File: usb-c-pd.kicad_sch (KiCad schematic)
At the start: 1 part, among them U1 CYPD3177-24LQ

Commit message: feat: add primary components
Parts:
- added J1: USB_C_Receptacle_PowerOnly_6P, symbol Connector:USB_C_Receptacle_PowerOnly_6P
- added J2: Barrel_Jack, symbol Connector:Barrel_Jack
- added U2: STM32G030K8Tx, Package_QFP:LQFP-32_7x7mm_P0.8mm, symbol MCU_ST_STM32G0:STM32G030K8Tx
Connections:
- new net: J1.A12 (GND), J1.B12 (GND)
- new net: J1.A9 (VBUS), J1.B9 (VBUS)
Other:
- moved on the sheet: U1

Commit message: feat: ez-pd
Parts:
- removed J2: Barrel_Jack, symbol Connector:Barrel_Jack
- added C1, C2: 1uF, symbol Device:C_Small
- added C3, C4: 0.1uF, symbol Device:C_Small
- added C5, C6: 4.7uF, symbol Device:C_Small
- added C7, C8, C9: 100nF, symbol Device:C_Small
- added D1: LED, symbol Device:LED
- added J2: Barrel_Jack_Switch, symbol Connector:Barrel_Jack_Switch
- added Q1: T2N7002AK, Package_TO_SOT_SMD:SOT-23, symbol Transistor_FET:T2N7002AK
- added Q2: ~, usb-c-pd-lib:SOIC127P600X175-8N, symbol usb-c-pd-prodj-lib:DMP3098LSD-13
- added R1, R3, R4: 4.7k, symbol Device:R_Small
- added R10, R11, R13, R15, R16, R17, R19, R6, R7, R8, R9: 2.2k, symbol Device:R_Small
- added R12: DNP, symbol Device:R_Small
- added R14: 20k, symbol Device:R_Small
- added R18: 12mR, symbol Device:R_Small
- added R2, R5: TODO, symbol Device:R_Small
- added U3: INA180A3, Package_TO_SOT_SMD:SOT-23-5, symbol Amplifier_Current:INA180A3
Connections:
- net VBUX_MIN: now reaches U1.1 (VBUS_MIN)
- net VBUX_MIN: now also R8.2, R9.1
- net at U1.10 (FLIP): now also R1.1
- net +VBUS_PD: now reaches U1.11 (VDC_OUT)
- net +VBUS_PD: now also C7.1, Q2.5 (D2), Q2.6 (D2), R18.2, U3.3 (+)
- net at U1.12 (HPI_SDA): now also R4.2
- net at U1.13 (HPI_SCL): now also R3.2
- net at U1.14 (CC2): now also J1.B5 (CC2)
- net at U1.15 (CC1): now also J1.A5 (CC1)
- net VBUS: now reaches U1.18 (VBUS_IN)
- net VBUS: now also J1.A9 (VBUS), J1.B9 (VBUS), C6.1, D1.2 (A), Q2.7 (D), Q2.8 (D), R14.1
- net GND: now reaches U1.19 (GND), U1.22 (GND), U1.25 (GND)
- net GND: now also J1.A12 (GND), J1.B12 (GND), J1.S1 (SHIELD), C1.2, C2.2, C3.2, C4.2, C5.2, C8.2, C9.1, J2.2, J2.3, Q1.2 (S), R11.2, R13.2, R5.1, R7.2, R9.2, U3.2 (GND)
- net VBUX_MAX: now reaches U1.2 (VBUS_MAX)
- net VBUX_MAX: now also R6.2, R7.1
- net +3V3: now reaches U1.23 (VDDD)
- net +3V3: now also C2.1, C3.1, C4.1, R1.2, R3.1, R4.1
- net at U1.24 (VCCD): now also C1.1
- net VBUS_FET_EN: now reaches U1.3 (VBUS_FET_EN)
- net VBUS_FET_EN: now also R16.2
- net at U1.4 (SAFE_PWR_EN): now also R17.1
- net ISINK_COARSE: now reaches U1.5 (ISNK_COARSE)
- net ISINK_COARSE: now also R10.2, R11.1
- net ISINK_FINE: now reaches U1.6 (ISNK_FINE)
- net ISINK_FINE: now also R12.2, R13.1
- net at U1.9 (FAULT): now also Q1.1 (G), R5.2
- new net: Q1.3 (D), R2.1
- new net: Q2.1 (S1), Q2.3 (S2)
- new net: Q2.2 (G1), Q2.4 (G2), R15.1
- new net: D1.1 (K), R2.2
- new net: R19.1, U3.1
- new net: C6.2, C7.2, R14.2, R15.2, R16.1
- new net +3V3 MCU: C8.1, R10.1, R12.1, R6.1, R8.1, U3.5 (V+)
- new net AMP_OUT: C9.2, R19.2
- new net PD_SAFE: R17.2
- new net VCONN: C5.1, J2.1, R18.1, U3.4 (-)
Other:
- note added: "ISINK = 3V3 * 0/2 -> 0A"
- note added: "ISINK = 3V3/2 -> 3A"
- note added: "VBUX_MAX = 3V3/2 -> 15V"
- note added: "VBUX_MIN = 3V3/2 -> 15V"
- note added: "Verify that this transistor is in stock"
- moved on the sheet: J1, U1

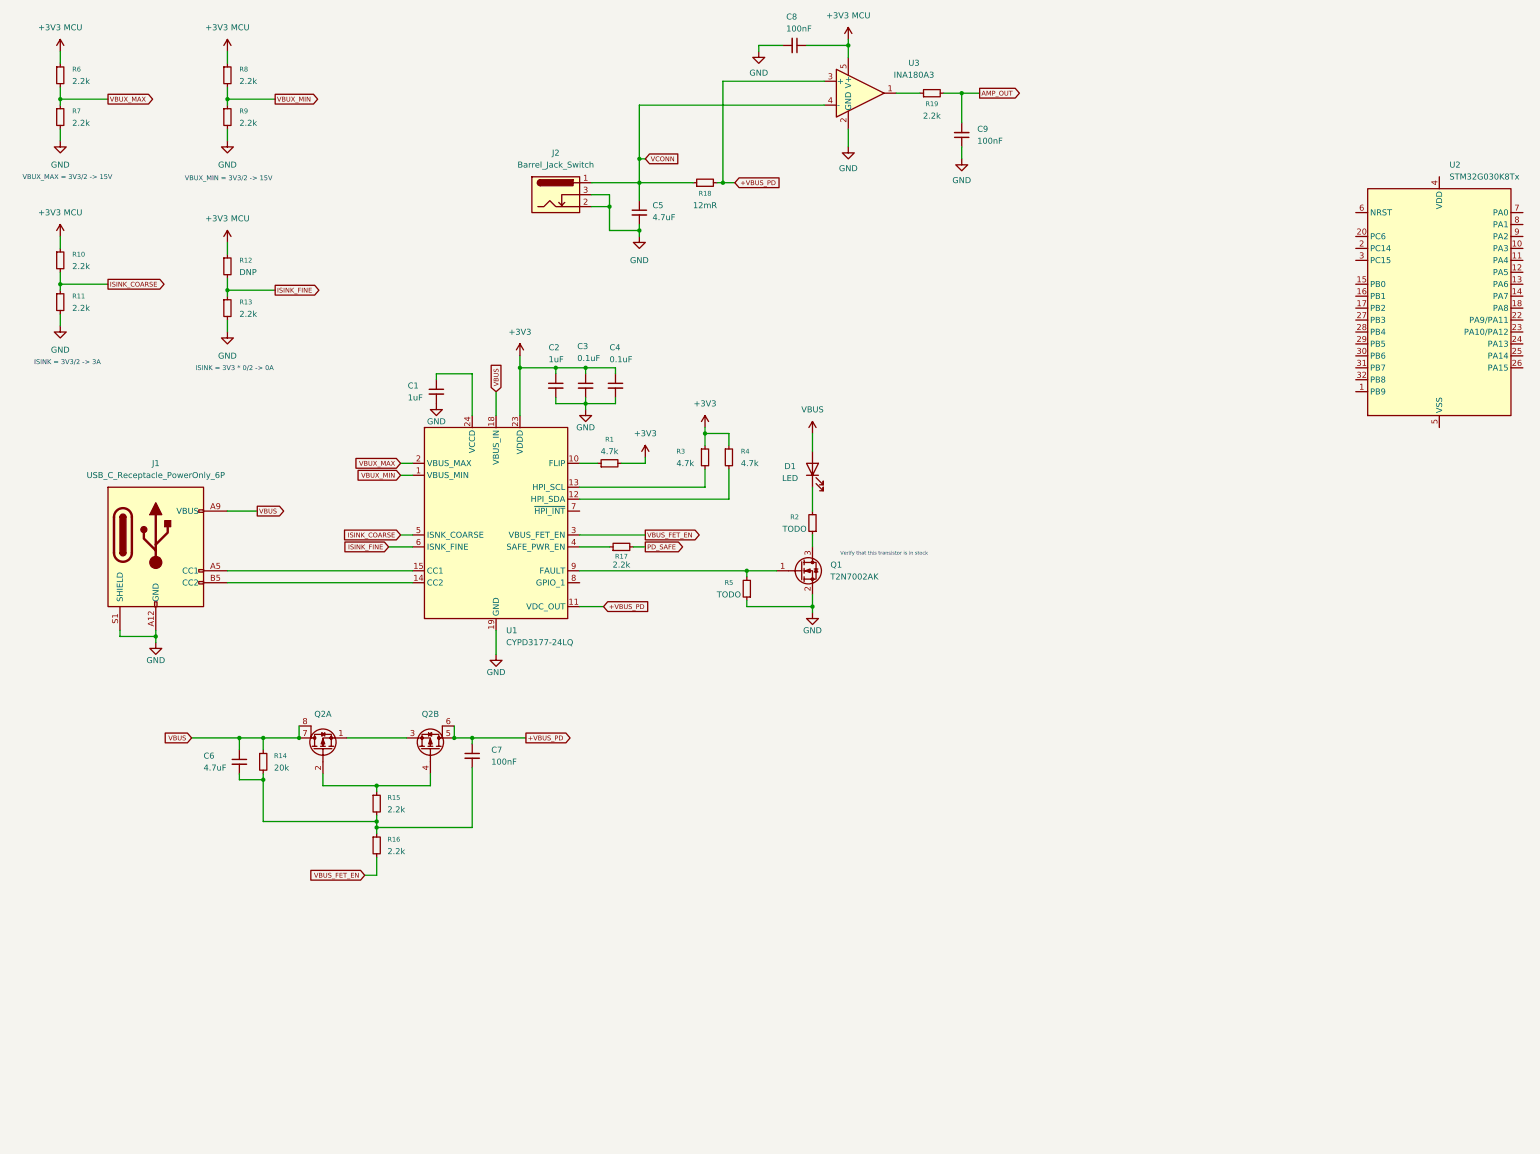
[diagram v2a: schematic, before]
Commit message: feat: mcu (#1)
* feat: stm mcu

* feat: SWO programming

* verify ERC
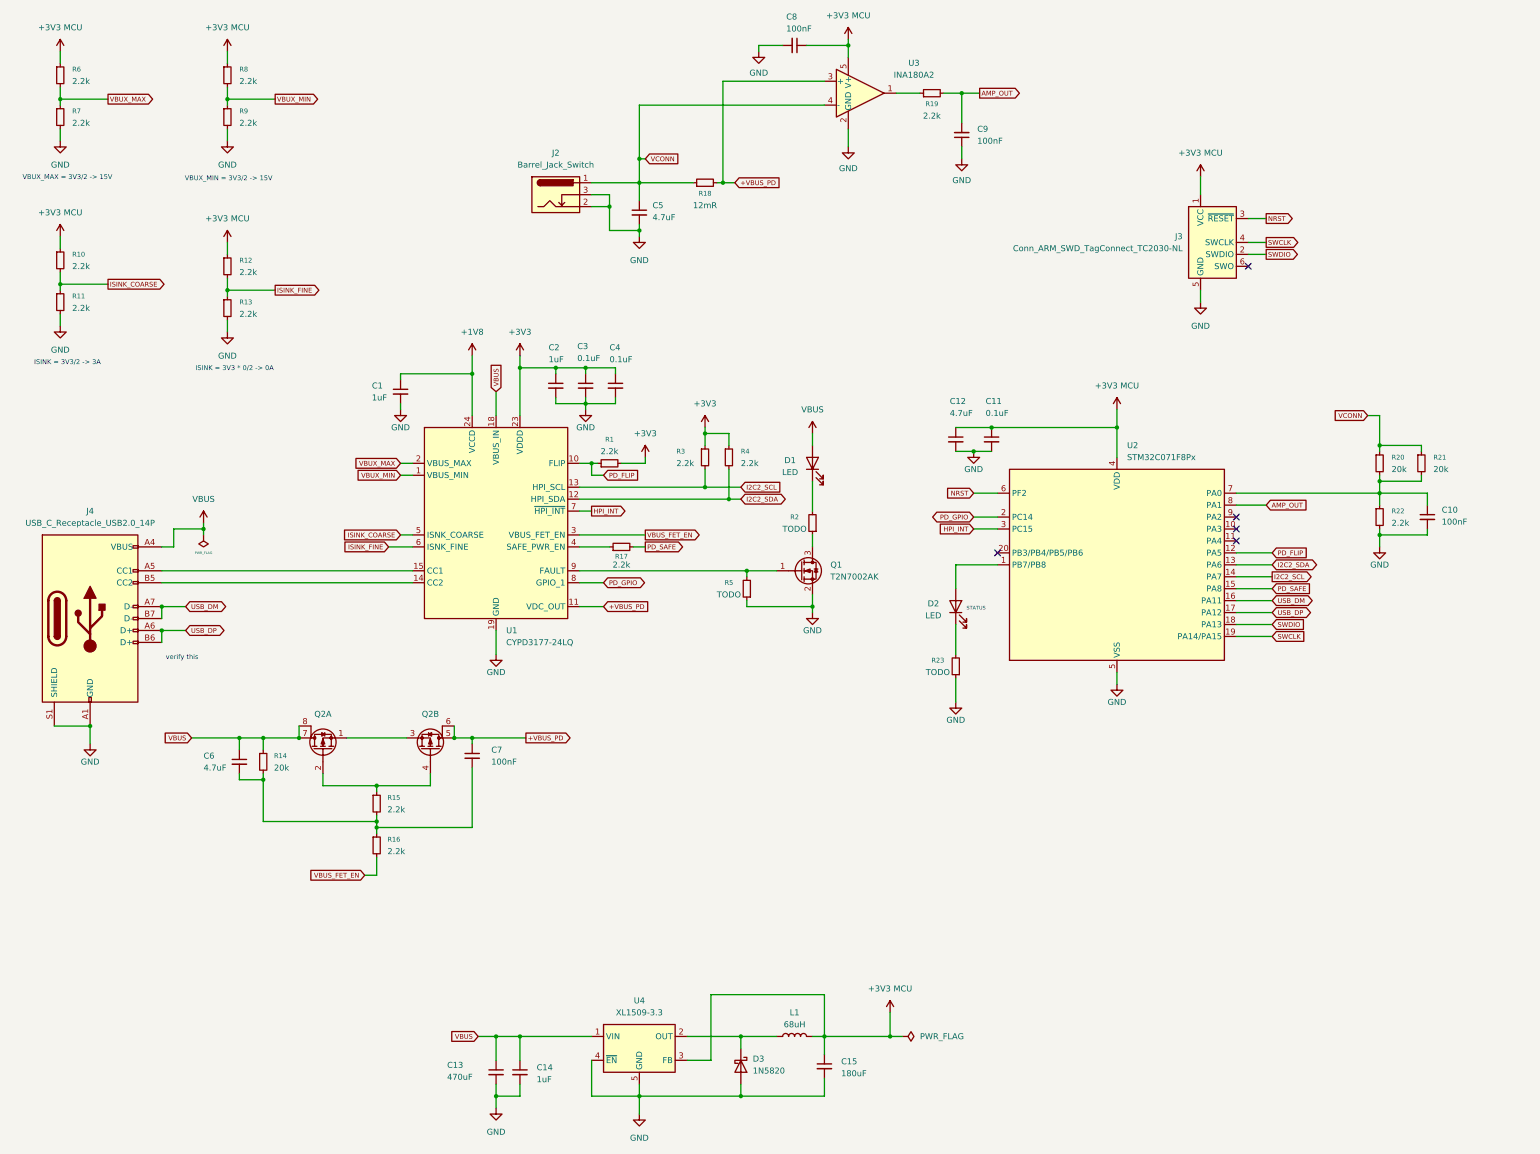
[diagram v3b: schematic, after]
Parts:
- removed J1: USB_C_Receptacle_PowerOnly_6P, symbol Connector:USB_C_Receptacle_PowerOnly_6P
- removed U2: STM32G030K8Tx, Package_QFP:LQFP-32_7x7mm_P0.8mm, symbol MCU_ST_STM32G0:STM32G030K8Tx
- removed U3: INA180A3, Package_TO_SOT_SMD:SOT-23-5, symbol Amplifier_Current:INA180A3
- added C10: 100nF, symbol Device:C_Small
- added C11: 0.1uF, symbol Device:C_Small
- added C12: 4.7uF, symbol Device:C_Small
- added C13: 470uF, symbol Device:C_Small
- added C14: 1uF, symbol Device:C_Small
- added C15: 180uF, symbol Device:C_Small
- added D2: LED, symbol Device:LED
- added D3: 1N5820, Diode_THT:D_DO-201AD_P15.24mm_Horizontal, symbol Diode:1N5820
- added J3: Conn_ARM_SWD_TagConnect_TC2030-NL, Connector:Tag-Connect_TC2030-IDC-NL_2x03_P1.27mm_Vertical, symbol Connector:Conn_ARM_SWD_TagConnect_TC2030-NL
- added J4: USB_C_Receptacle_USB2.0_14P, symbol Connector:USB_C_Receptacle_USB2.0_14P
- added L1: 68uH, symbol Device:L
- added R20, R21: 20k, Resistor_SMD:R_0603_1608Metric_Pad0.98x0.95mm_HandSolder, symbol Device:R_Small
- added R22: 2.2k, Resistor_SMD:R_0603_1608Metric_Pad0.98x0.95mm_HandSolder, symbol Device:R_Small
- added R23: TODO, Resistor_SMD:R_0603_1608Metric_Pad0.98x0.95mm_HandSolder, symbol Device:R_Small
- added U2: STM32C071F8Px, Package_SO:TSSOP-20_4.4x6.5mm_P0.65mm, symbol MCU_ST_STM32C0:STM32C071F8Px
- added U3: INA180A2, Package_TO_SOT_SMD:SOT-23-5, symbol Amplifier_Current:INA180A2
- added U4: XL1509-3.3, Package_SO:SOIC-8_3.9x4.9mm_P1.27mm, symbol Regulator_Switching:XL1509-3.3
- R1, R3, R4: value 4.7k -> 2.2k; footprint (none) -> Resistor_SMD:R_0603_1608Metric_Pad0.98x0.95mm_HandSolder
- R10, R11, R13, R14, R15, R16, R17, R19, R2, R5, R6, R7, R8, R9: footprint (none) -> Resistor_SMD:R_0603_1608Metric_Pad0.98x0.95mm_HandSolder
- R12: value DNP -> 2.2k; footprint (none) -> Resistor_SMD:R_0603_1608Metric_Pad0.98x0.95mm_HandSolder
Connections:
- net +3V3 MCU: now also C11.1, C12.1, C15.1, J3.1 (VCC), L1.2, U2.4 (VDD), U3.5 (V+), U4.3 (FB)
- net +VBUS_PD: now also U3.3 (+)
- net AMP_OUT: now also U2.8 (PA1)
- net GND: now also C10.2, C11.2, C12.2, C13.2, C14.2, C15.2, D3.2 (A), J3.5 (GND), J4.A1 (GND), J4.A12 (GND), J4.B1 (GND), J4.B12 (GND), J4.S1 (SHIELD), R22.2, R23.1, U2.5 (VSS), U3.2 (GND), U4.4 (~{EN}), U4.5 (GND), U4.6 (GND), U4.7 (GND), U4.8 (GND)
- net PD_SAFE: now also U2.15 (PA8)
- net VBUS: now also C13.1, C14.1, J4.A4 (VBUS), J4.A9 (VBUS), J4.B4 (VBUS), J4.B9 (VBUS), U4.1 (VIN)
- net VCONN: now also R20.1, R21.1, U3.4 (-)
- net I2C2_SDA: now reaches R4.2, U1.12 (HPI_SDA)
- net I2C2_SDA: now also U2.13 (PA6)
- net +1V8: now reaches C1.1, U1.24 (VCCD)
- net PD_FLIP: now reaches R1.1, U1.10 (FLIP)
- net PD_FLIP: now also U2.12 (PA5)
- net at R19.1: now also U3.1
- net I2C2_SCL: now reaches R3.2, U1.13 (HPI_SCL)
- net I2C2_SCL: now also U2.14 (PA7)
- net at U1.14 (CC2): now also J4.B5 (CC2)
- net at U1.15 (CC1): now also J4.A5 (CC1)
- net HPI_INT: now reaches U1.7 (~{HPI_INT})
- net HPI_INT: now also U2.3 (PC15)
- net PD_GPIO: now reaches U1.8 (GPIO_1)
- net PD_GPIO: now also U2.2 (PC14)
- new net: C10.1, R20.2, R21.2, R22.1, U2.7 (PA0)
- new net: D2.1 (K), R23.2
- new net: D2.2 (A), U2.1 (PB7/PB8)
- new net: D3.1 (K), L1.1, U4.2 (OUT)
- new net NRST: J3.3 (~{RESET}), U2.6 (PF2)
- new net SWCLK: J3.4 (SWCLK), U2.19 (PA14/PA15)
- new net SWDIO: J3.2 (SWDIO), U2.18 (PA13)
- new net USB_DM: J4.A7 (D-), J4.B7 (D-), U2.16 (PA11)
- new net USB_DP: J4.A6 (D+), J4.B6 (D+), U2.17 (PA12)
- no-connect marks 0 -> 5
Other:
- note added: "STATUS"
- note added: "verify this"
- note removed: "Verify that this transistor is in stock"
- moved on the sheet: C1, D1

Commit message: feat: configure footprints
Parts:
- C1, C11, C12, C13, C14, C15, C2, C3, C4, C5, C6: footprint (none) -> Capacitor_SMD:C_0603_1608Metric_Pad1.08x0.95mm_HandSolder
- C10, C7, C8, C9: value 100nF -> 0.1uF; footprint (none) -> Capacitor_SMD:C_0603_1608Metric_Pad1.08x0.95mm_HandSolder
- D1, D2: footprint (none) -> Diode_SMD:D_0603_1608Metric_Pad1.05x0.95mm_HandSolder
- J2: footprint (none) -> usb-c-pd-lib:PJ002AHSMTTR
- L1: footprint (none) -> Inductor_SMD:L_0603_1608Metric_Pad1.05x0.95mm_HandSolder
- R18: footprint (none) -> Resistor_SMD:R_0603_1608Metric_Pad0.98x0.95mm_HandSolder
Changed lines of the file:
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@@
 		)
 	)
-	(global_label "VBUS"
-		(shape input)
-		(at 119.38 97.79 90)
-		(fields_autoplaced yes)
-		(effects
-			(font
-				(size 1.016 1.016)
-			)
-			(justify left)
-		)
-		(property "Intersheetrefs" "${INTERSHEET_REFS}"
-			(at 119.38 91.4832 90)
-			(effects
-				(font
-					(size 1.27 1.27)
-				)
-				(justify left)
-				(hide yes)
-			)
-		)
-	)
 	(global_label "HPI_INT"
 		(shape output)
@@
 			)
 		)
-		(property "Footprint" ""
+		(property "Footprint" "Capacitor_SMD:C_0603_1608Metric_Pad1.08x0.95mm_HandSolder"
 			(at 138.43 96.52 0)
 			(effects
@@
 			)
 		)
-		(property "Footprint" ""
+		(property "Footprint" "Capacitor_SMD:C_0603_1608Metric_Pad1.08x0.95mm_HandSolder"
 			(at 99.06 97.79 0)
 			(effects
@@
 			)
 		)
-		(property "Footprint" ""
+		(property "Footprint" "Diode_SMD:D_0603_1608Metric_Pad1.05x0.95mm_HandSolder"
 			(at 217.17 143.51 0)
 			(effects
@@
 			)
 		)
-		(property "Value" "100nF"
+		(property "Value" "0.1uF"
 			(at 181.102 20.574 90)
 			(effects
@@
 			)
 		)
-		(property "Footprint" ""
+		(property "Footprint" "Capacitor_SMD:C_0603_1608Metric_Pad1.08x0.95mm_HandSolder"
 			(at 182.88 24.13 0)
 			(effects
@@
 			)
 		)
-		(property "Value" "100nF"
+		(property "Value" "0.1uF"
 			(at 320.548 125.476 0)
 			(effects
@@
 			)
 		)
-		(property "Footprint" ""
+		(property "Footprint" "Capacitor_SMD:C_0603_1608Metric_Pad1.08x0.95mm_HandSolder"
 			(at 317.5 124.46 0)
 			(effects
@@
 			)
 		)
-		(property "Footprint" ""
+		(property "Footprint" "Capacitor_SMD:C_0603_1608Metric_Pad1.08x0.95mm_HandSolder"
 			(at 217.17 107.95 0)
 			(effects
@@
 			)
 		)
-		(property "Footprint" ""
+		(property "Footprint" "Capacitor_SMD:C_0603_1608Metric_Pad1.08x0.95mm_HandSolder"
 			(at 132.08 96.52 0)
 			(effects
@@
 			)
 		)
-		(property "Footprint" ""
+		(property "Footprint" "Capacitor_SMD:C_0603_1608Metric_Pad1.08x0.95mm_HandSolder"
 			(at 189.23 241.3 0)
 			(effects
@@
 			)
 		)
-		(property "Footprint" ""
+		(property "Footprint" "Capacitor_SMD:C_0603_1608Metric_Pad1.08x0.95mm_HandSolder"
 			(at 119.38 242.57 0)
 			(effects
@@
 			)
 		)
-		(property "Footprint" ""
+		(property "Footprint" "Capacitor_SMD:C_0603_1608Metric_Pad1.08x0.95mm_HandSolder"
 			(at 144.78 96.52 0)
 			(effects
@@
 	)
 	(symbol
+		(lib_id "power:VBUS")
+		(at 119.38 97.79 0)
+		(unit 1)
+		(exclude_from_sim no)
+		(in_bom yes)
+		(on_board yes)
+		(dnp no)
+		(fields_autoplaced yes)
+		(property "Reference" "#PWR035"
+			(at 119.38 101.6 0)
+			(effects
+				(font
+					(size 1.27 1.27)
+				)
+				(hide yes)
+			)
+		)
+		(property "Value" "VBUS"
+			(at 119.38 92.71 0)
+			(effects
+				(font
+					(size 1.27 1.27)
+				)
+			)
+		)
+		(property "Footprint" ""
+			(at 119.38 97.79 0)
+			(effects
+				(font
+					(size 1.27 1.27)
+				)
+				(hide yes)
+			)
+		)
+		(property "Datasheet" ""
+			(at 119.38 97.79 0)
+			(effects
+				(font
+					(size 1.27 1.27)
+				)
+				(hide yes)
+			)
+		)
+		(property "Description" "Power symbol creates a global label with name \"VBUS\""
+			(at 119.38 97.79 0)
+			(effects
+				(font
+					(size 1.27 1.27)
+				)
+				(hide yes)
+			)
+		)
+		(pin "1"
+		)
+		(instances
+			(project "usb-c-pd"
+				(path "/8b91f438-df16-4abb-b457-7ba42e3c4b7f"
+					(reference "#PWR035")
+					(unit 1)
+				)
+			)
+		)
+	)
+	(symbol
 		(lib_id "Connector:USB_C_Receptacle_USB2.0_14P")
 		(at 33.02 146.05 0)
@@
 			)
 		)
-		(property "Value" "100nF"
+		(property "Value" "0.1uF"
 			(at 118.364 176.53 0)
 			(effects
@@
 			)
 		)
-		(property "Footprint" ""
+		(property "Footprint" "Capacitor_SMD:C_0603_1608Metric_Pad1.08x0.95mm_HandSolder"
 			(at 114.3 175.26 0)
 			(effects
@@
 			)
 		)
-		(property "Footprint" ""
+		(property "Footprint" "usb-c-pd-lib:PJ002AHSMTTR"
 			(at 133.35 56.896 0)
 			(effects
@@
 			)
 		)
-		(property "Footprint" ""
+		(property "Footprint" "Inductor_SMD:L_0603_1608Metric_Pad1.05x0.95mm_HandSolder"
 			(at 182.88 234.95 0)
 			(effects
@@
 			)
 		)
-		(property "Footprint" ""
+		(property "Footprint" "Capacitor_SMD:C_0603_1608Metric_Pad1.08x0.95mm_HandSolder"
 			(at 224.79 107.95 0)
 			(effects
@@
 			)
 		)
-		(property "Footprint" ""
+		(property "Footprint" "Capacitor_SMD:C_0603_1608Metric_Pad1.08x0.95mm_HandSolder"
 			(at 124.46 242.57 0)
 			(effects
@@
 			)
 		)
-		(property "Footprint" ""
+		(property "Footprint" "Diode_SMD:D_0603_1608Metric_Pad1.05x0.95mm_HandSolder"
 			(at 186.69 113.03 0)
 			(effects
@@
 			)
 		)
-		(property "Value" "100nF"
+		(property "Value" "0.1uF"
 			(at 221.742 44.45 0)
 			(effects
@@
 			)
 		)
-		(property "Footprint" ""
+		(property "Footprint" "Capacitor_SMD:C_0603_1608Metric_Pad1.08x0.95mm_HandSolder"
 			(at 218.44 43.18 0)
 			(effects
@@
 			)
 		)
-		(property "Footprint" ""
+		(property "Footprint" "Capacitor_SMD:C_0603_1608Metric_Pad1.08x0.95mm_HandSolder"
 			(at 64.77 176.53 0)
 			(effects
@@
 			)
 		)
-		(property "Footprint" ""
+		(property "Footprint" "Capacitor_SMD:C_0603_1608Metric_Pad1.08x0.95mm_HandSolder"
 			(at 149.86 59.69 0)
 			(effects
@@
 			)
 		)
-		(property "Footprint" ""
+		(property "Footprint" "Resistor_SMD:R_0603_1608Metric_Pad0.98x0.95mm_HandSolder"
 			(at 163.83 53.34 0)
 			(effects
